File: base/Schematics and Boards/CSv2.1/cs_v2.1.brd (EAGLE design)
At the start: 38.1 x 47 mm, 77 parts, among them J101 J-JTAG-CORTEX-NEEDLE6-LEGS, J301 HIROSE-DF40_50-PIN_CONNECTORS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, J302 HIROSE-DF40_50-PIN_CONNECTORS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, Q1 DMG3415UFY4Q-7F, U1 NCP708MU330TAG, U101 ATSAMD51, U2 W25N01GVZEIG, U201 COULOMB-MAX17262, U202 MAX77827BEWC+T, U203 SENSOR-SI7006, U204 LOADSWITCH-MIC94164, U205 LOADSWITCH-MIC94164, U3 TS3A24159YZPR, U4 LOADSWITCH-MIC94164, U5 PD3S140-7, Y102 ABS07-32.768KHZ-9-T

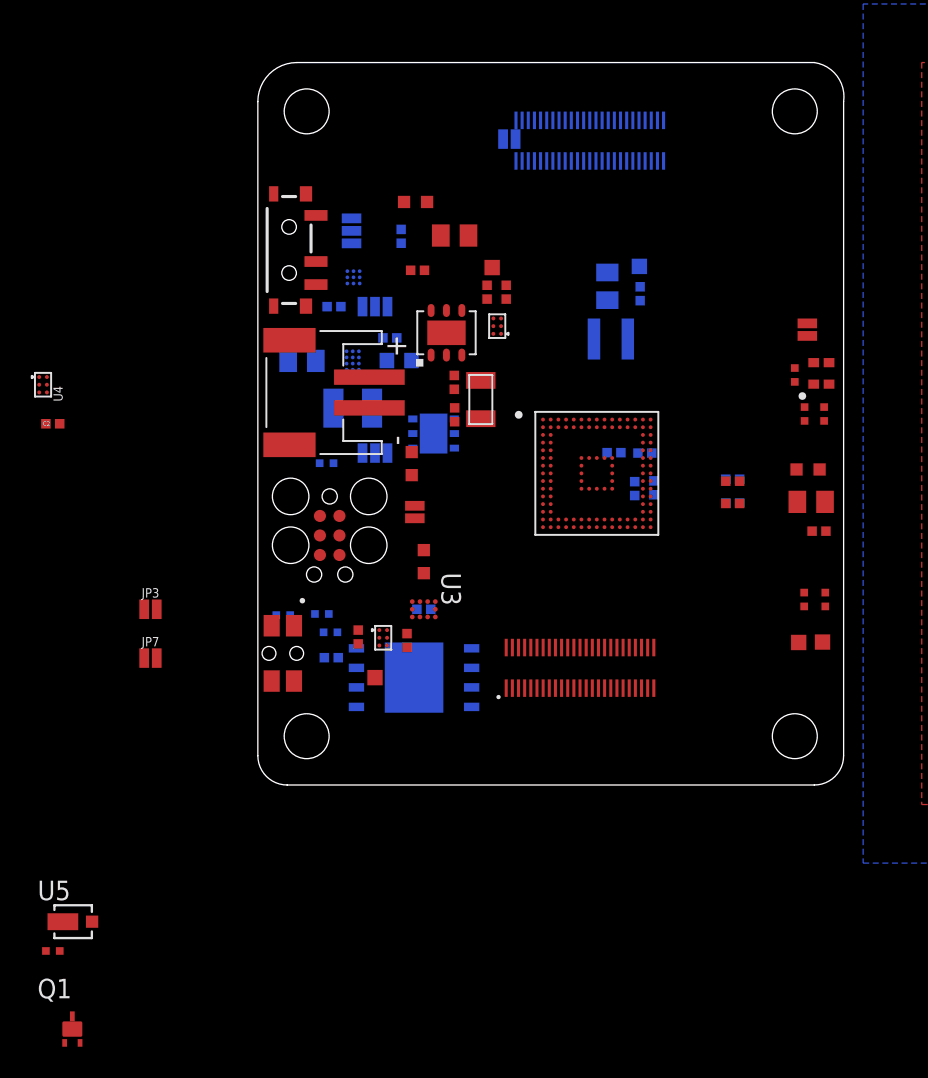
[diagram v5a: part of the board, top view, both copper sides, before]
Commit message: CSv2.1 main board part placement; routing for power traces
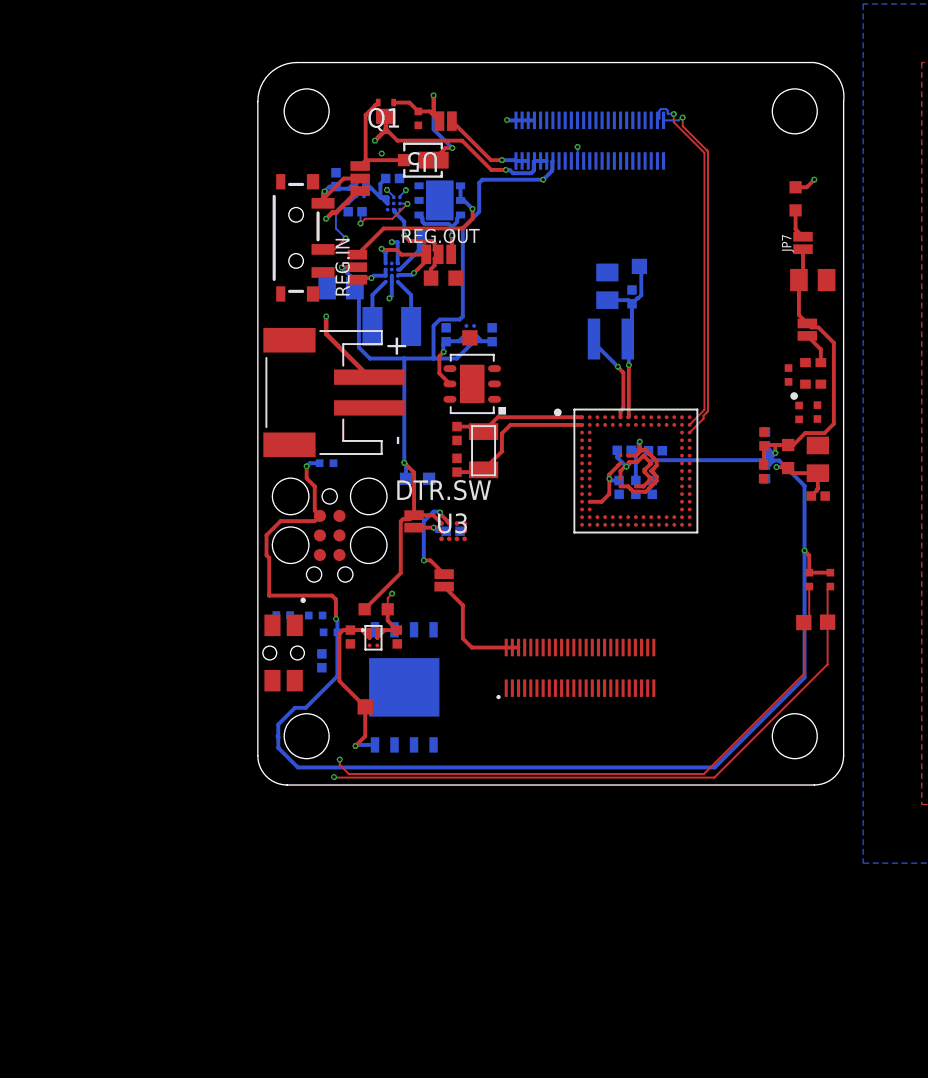
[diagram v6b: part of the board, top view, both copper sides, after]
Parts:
- removed JP1, JP2: JUMPER-SMT_3_1-NC_PASTE_NO-SILK, SparkFun-Jumpers:SMT-JUMPER_3_1-NC_PASTE_NO-SILK
- removed JP3: JUMPER-SMT_2_NC_PASTE_NO-SILK, Connectors:SMT-JUMPER_2_NC_PASTE_NO-SILK
- added DTR.SW: JUMPER-SMT_2_NC_PASTE_NO-SILK, Connectors:SMT-JUMPER_2_NC_PASTE_NO-SILK
- added REG.IN, REG.OUT: JUMPER-SMT_3_1-NC_PASTE_NO-SILK, SparkFun-Jumpers:SMT-JUMPER_3_1-NC_PASTE_NO-SILK
- moved Q1 62.8 mm to (8.33, 43.5), turned to 180 degrees
- moved R1 59.1 mm to (10.4, 43.4), turned to 90 degrees
- moved U5 54.0 mm to (10.2, 40.6), turned to 180 degrees
- moved JP7 50.3 mm to (35.5, 35.3), turned to 90 degrees
- moved R206 24.7 mm to (35.0, 38.1), turned to 270 degrees
- moved C2 24.3 mm to (5.08, 39.4), flipped to the bottom, turned to 90 degrees
- moved U4 24.2 mm to (6.65, 38.8), flipped to the bottom
- moved C115 23.5 mm to (36.1, 32.8), turned to 0 degrees
- moved C114 17.8 mm to (23.8, 21.8), flipped to the bottom, turned to 0 degrees
- moved U1 15.2 mm to (11.8, 38.0), turned to 180 degrees
- moved C204 6.63 mm to (10.6, 35.4), turned to 90 degrees
- moved C203 6.32 mm to (6.32, 37.3)
- moved U202 6.25 mm to (8.71, 33.3)
- moved C202 6.08 mm to (12.1, 33.0), flipped to the top, turned to 0 degrees
- moved L201 5.88 mm to (8.71, 29.8)
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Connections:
- net VREG_LX1 renamed BB_LX1
- net VREG_LX2 renamed BB_LX2
- removed net N$15: JP2.3, U1.4, U1.5
- removed net N$3: JP2.1, U202.C2, U202.C3
- removed net N$7: JP1.3, U1.1, U1.6
- new net BB_REG_OUT: REG.IN.1, U202.C2, U202.C3
- new net LDO_REG_OUT: REG.IN.3, U1.4, U1.5
- new net REG_LDO_IN: REG.OUT.3, U1.1, U1.6
- net +3V3: now also DTR.SW.2, REG.IN.2; no longer JP2.2, JP3.2
- net N$17: now also DTR.SW.1; no longer JP3.1
- net VREG_BB_IN: now also REG.OUT.1; no longer JP1.1
- net VREG_IN: now also REG.OUT.2; no longer JP1.2
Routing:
- net +3V3_PROC: track 0.00 -> 128.0 mm, vias 0 -> 5
- net DTR_MSTR_I2C_SCL_SERCOM7_P1: track 0.00 -> 81.5 mm, vias 0 -> 2
- net DTR_MSTR_I2C_SDA_SERCOM7_P0: track 0.00 -> 80.0 mm, vias 0 -> 2
- net +3V3: track 0.00 -> 77.4 mm, vias 0 -> 4
- net DBG_STOR_V_SENSE: track 0.00 -> 51.4 mm, vias 0 -> 3
- net +3V7_BATT: track 0.00 -> 34.2 mm, vias 0 -> 4
- net DBG_USB_D_P: track 0.00 -> 23.4 mm, vias 0 -> 1
- net DBG_USB_D_N: track 0.00 -> 23.0 mm, vias 0 -> 1
- net VDDANA: track 0.00 -> 20.8 mm, vias 0 -> 2
- net +3V3_STOR: track 0.00 -> 13.5 mm, vias 0 -> 1
- net GND: track 0.00 -> 12.5 mm, vias 0 -> 4
- net VDDCORE: track 0.00 -> 12.0 mm, vias 0 -> 1
- net LDO_REG_OUT: track 0.00 -> 11.1 mm, vias 0 -> 1
- net V_SEL_IN_B: track 0.00 -> 10.2 mm, vias 0 -> 2
- net XOUT32: track 0.00 -> 10.1 mm
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
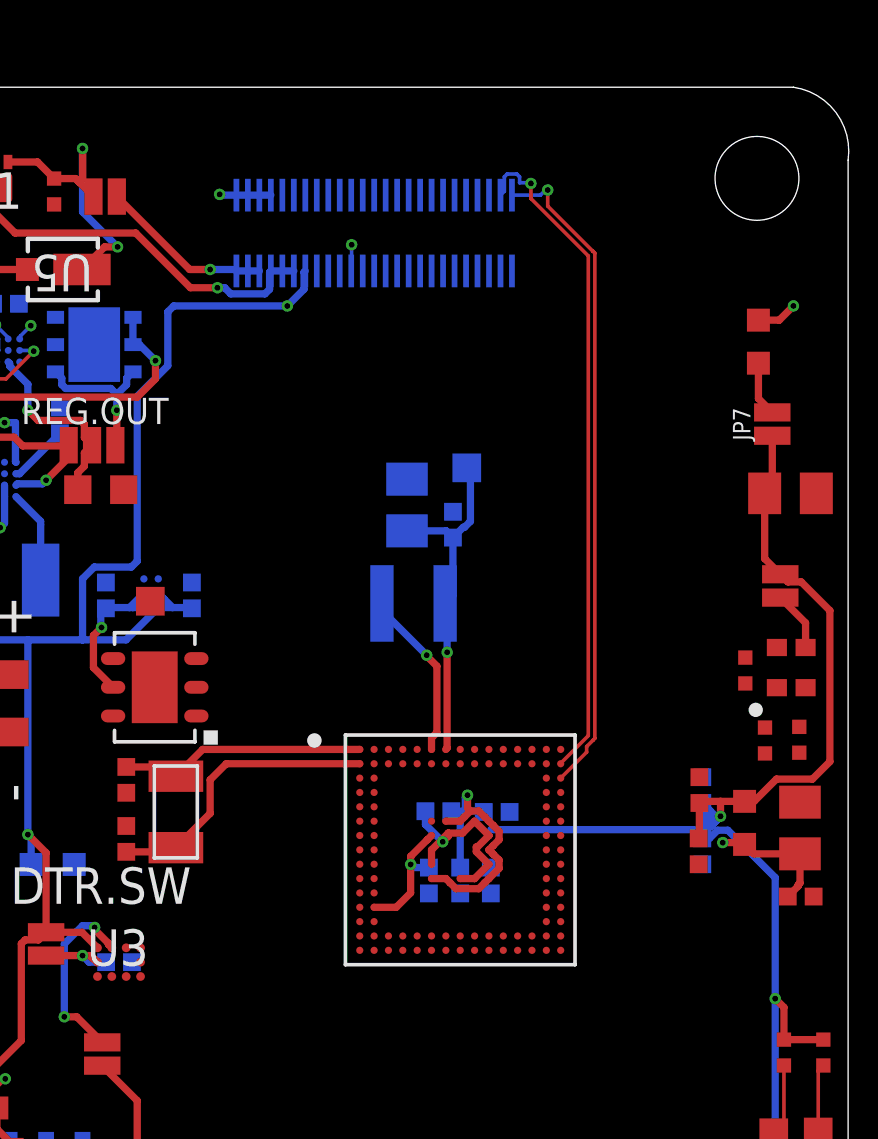
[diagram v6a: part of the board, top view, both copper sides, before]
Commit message: Move processor to make routing to connectors easier
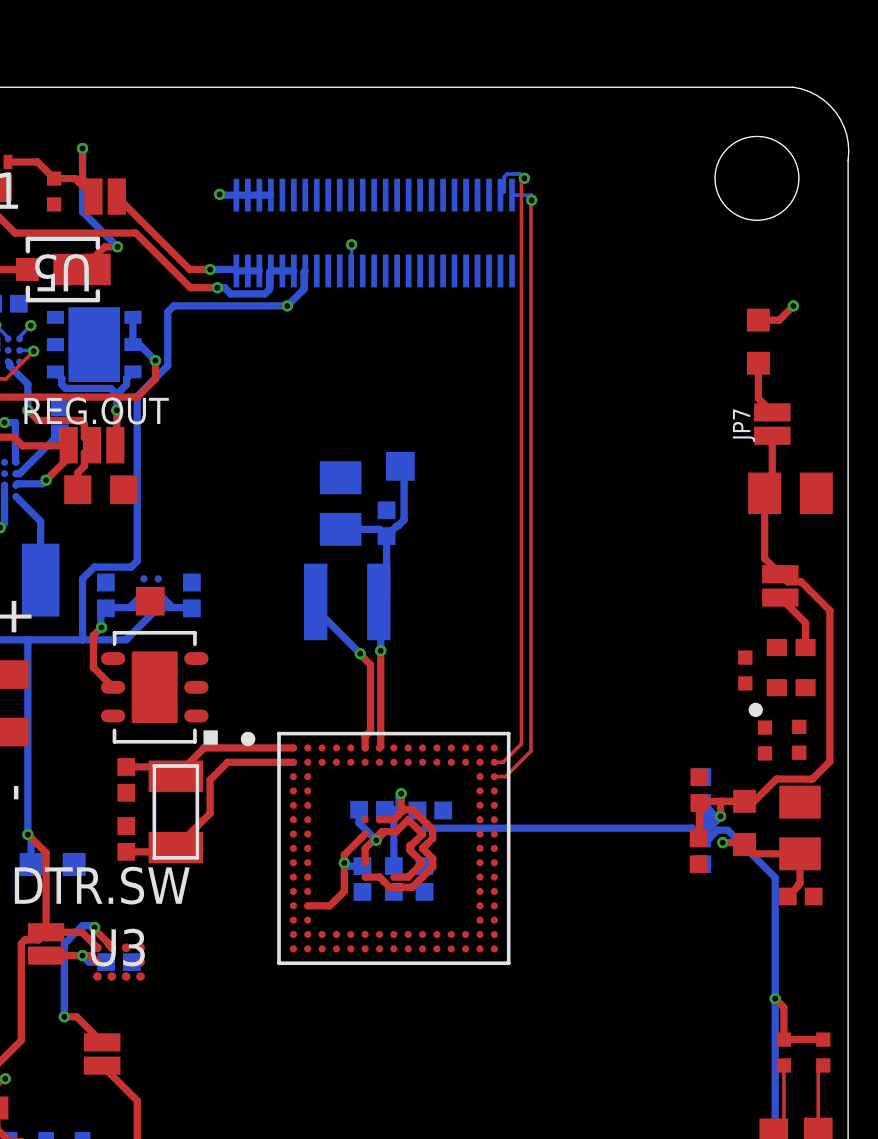
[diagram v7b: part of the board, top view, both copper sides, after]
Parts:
- moved C103 2.31 mm to (22.0, 31.8)
- moved C105 2.31 mm to (21.2, 19.4)
- moved C107 2.31 mm to (20.4, 32.5)
- moved C111 2.31 mm to (22.3, 19.4)
- moved C112 2.31 mm to (23.5, 21.8)
- moved C113 2.31 mm to (23.3, 19.4)
- moved C114 2.31 mm to (21.5, 21.8)
- moved L101 2.31 mm to (20.7, 29.1)
- moved U101 2.31 mm to (22.3, 20.5)
- moved CPU 2.31 mm to (22.5, 33.8)
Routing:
- net +3V3_PROC: track 128.0 -> 130.4 mm
- net VDDANA: track 20.8 -> 23.1 mm
- net XIN32: track 8.65 -> 6.36 mm
- net XOUT32: track 10.1 -> 7.80 mm
- net DBG_USB_D_N: track 23.0 -> 21.7 mm
- net DBG_USB_D_P: track 23.4 -> 22.5 mm

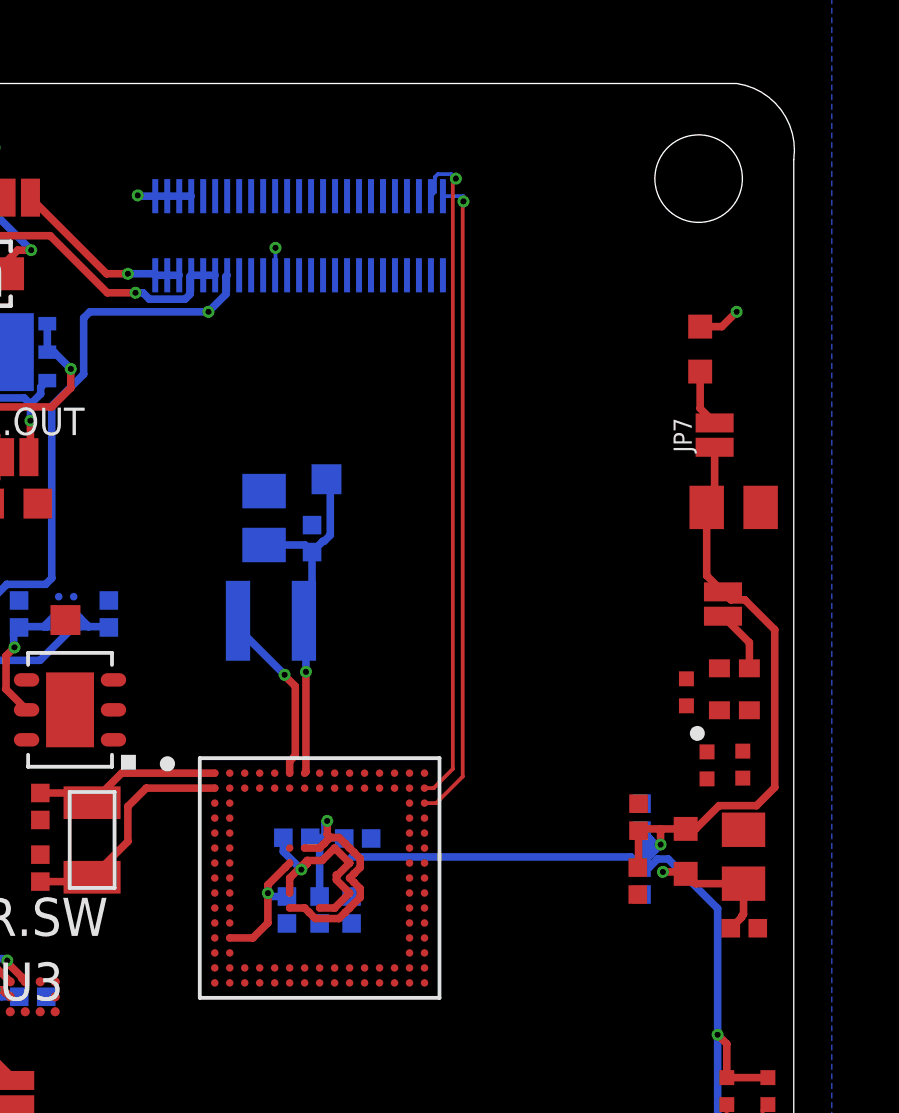
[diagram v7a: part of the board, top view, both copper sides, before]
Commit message: Re-jumble processor power traces and caps to make routing easier
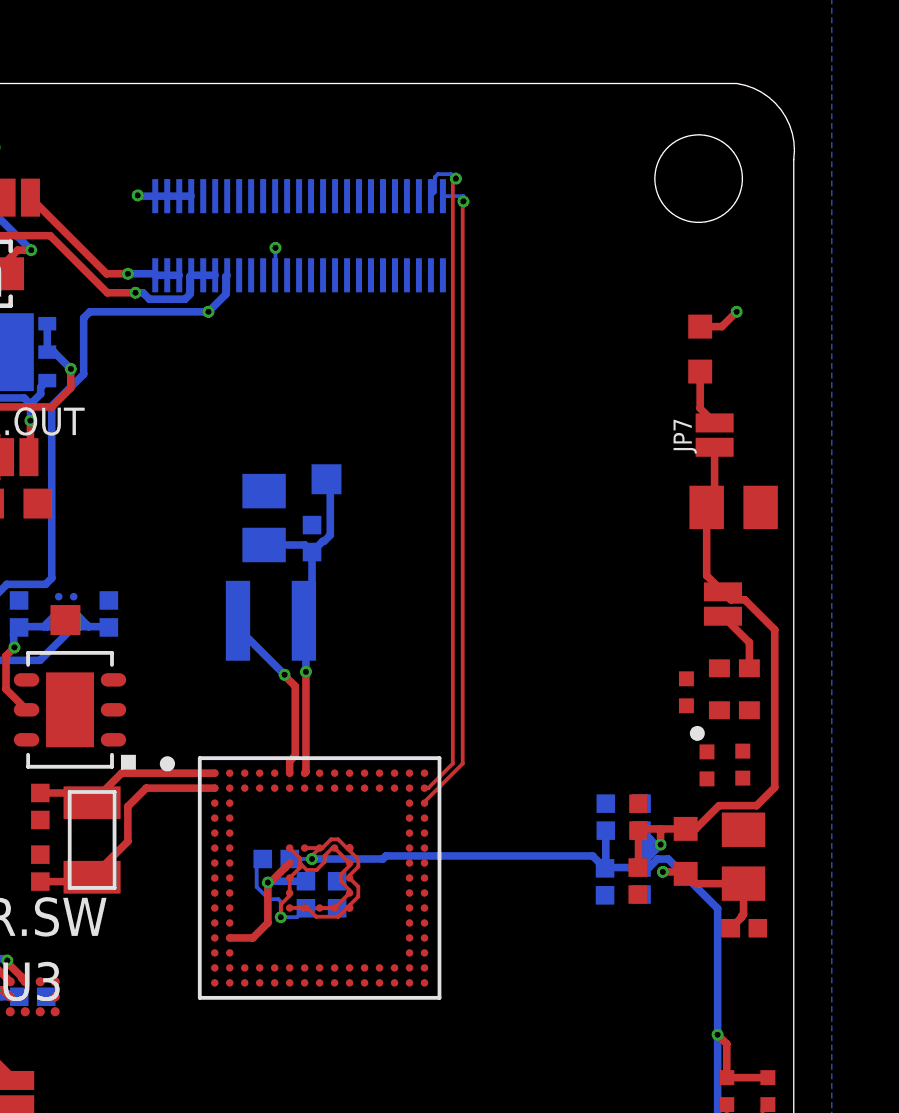
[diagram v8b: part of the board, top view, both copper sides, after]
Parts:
- moved C114 10.3 mm to (31.8, 22.5), turned to 90 degrees
- moved C112 8.38 mm to (31.8, 20.3), turned to 270 degrees
- moved C113 3.04 mm to (20.8, 21.1), turned to 0 degrees
- moved C105 0.81 mm to (21.8, 19.9)
- moved C111 0.77 mm to (22.9, 19.9)
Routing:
- net GND: track 12.5 -> 17.2 mm
- net +3V3_PROC: track 130.4 -> 129.6 mm
